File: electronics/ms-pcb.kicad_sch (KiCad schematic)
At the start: 38 parts, among them J1 Left motor, J2 Right motor, J3 XT60-M, U1 ESP32-S3-DEVKITC-1U-N8R2, U2 GY-521

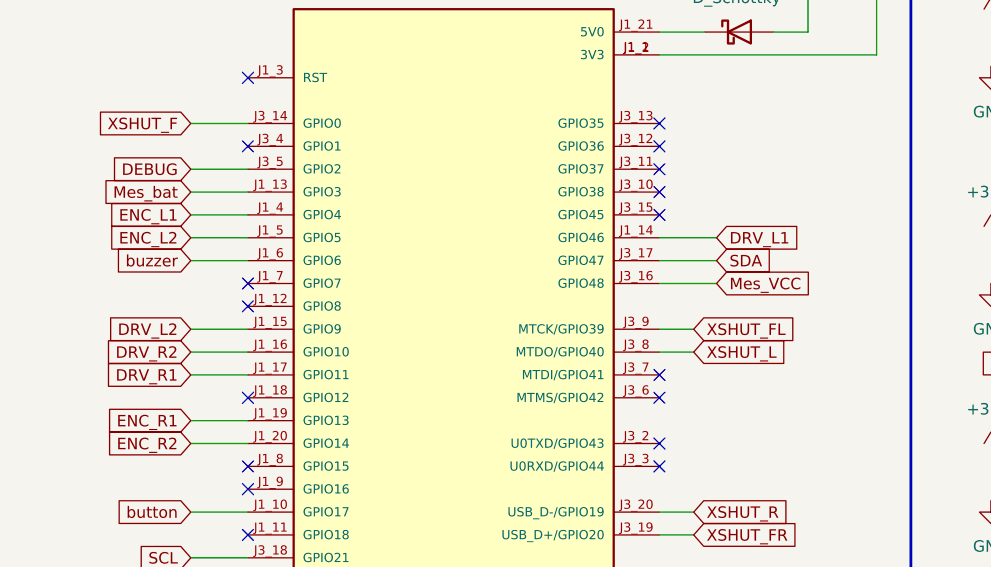
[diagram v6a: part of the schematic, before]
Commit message: elec: fix vcc voltage measurement pin
Closes: #66
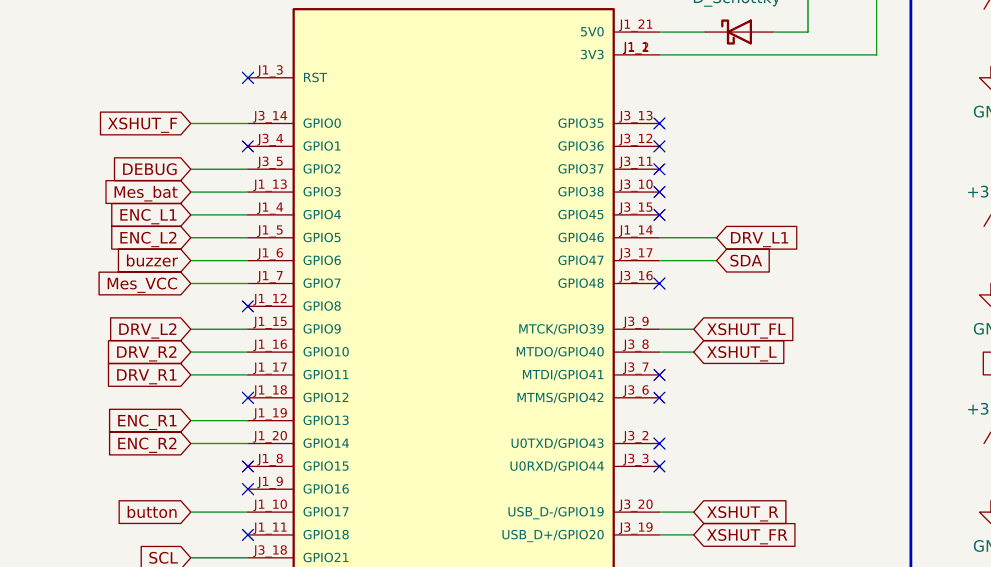
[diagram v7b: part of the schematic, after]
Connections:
- net Mes_VCC: now also U1.J1_7 (GPIO7); no longer U1.J3_16 (GPIO48)
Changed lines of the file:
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@@
-	)
-	(no_connect
-		(at 36.83 58.42)
 	)
 	(no_connect
@@
 	)
 	(no_connect
+		(at 82.55 58.42)
+	)
+	(no_connect
 		(at 20.32 135.89)
 	)
@@
 		(pts
 			(xy 95.25 180.34) (xy 95.25 185.42)
+		)
+		(stroke
+			(width 0)
+			(type default)
+		)
+	)
+	(wire
+		(pts
+			(xy 30.48 58.42) (xy 36.83 58.42)
 		)
 		(stroke
@@
 		(pts
 			(xy 152.4 147.32) (xy 152.4 151.13)
-		)
-		(stroke
-			(width 0)
-			(type default)
-		)
-	)
-	(wire
-		(pts
-			(xy 82.55 58.42) (xy 88.9 58.42)
 		)
 		(stroke
@@
 	(global_label "Mes_VCC"
 		(shape input)
-		(at 88.9 58.42 0)
+		(at 30.48 58.42 180)
 		(fields_autoplaced yes)
 		(effects
@@
 				(size 1.27 1.27)
 			)
-			(justify left)
+			(justify right)
 		)
 		(property "Intersheetrefs" "${INTERSHEET_REFS}"
-			(at 100.0495 58.42 0)
+			(at 19.3305 58.42 0)
 			(effects
 				(font
 					(size 1.27 1.27)
 				)
-				(justify left)
+				(justify right)
 				(hide yes)
 			)
